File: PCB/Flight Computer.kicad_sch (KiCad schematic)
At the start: 0 parts

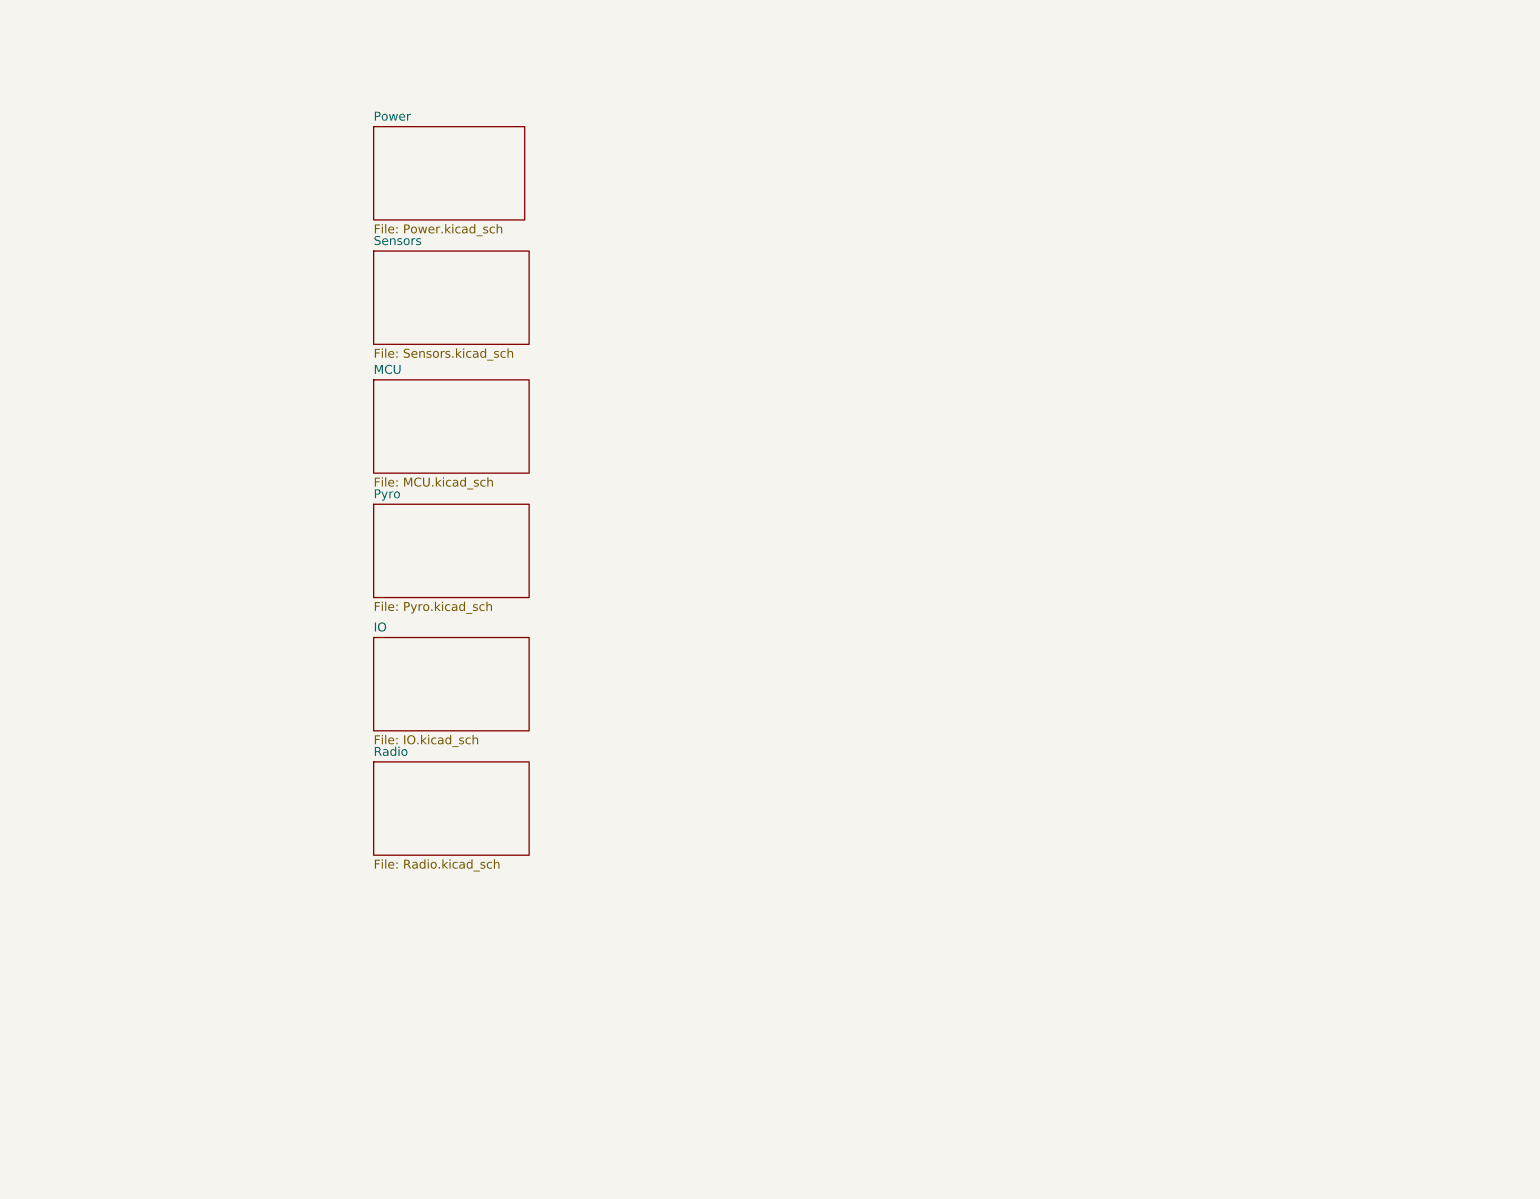
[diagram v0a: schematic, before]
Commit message: Cleaned up the schematic and replace and rerouted everything, also replace radio with a module
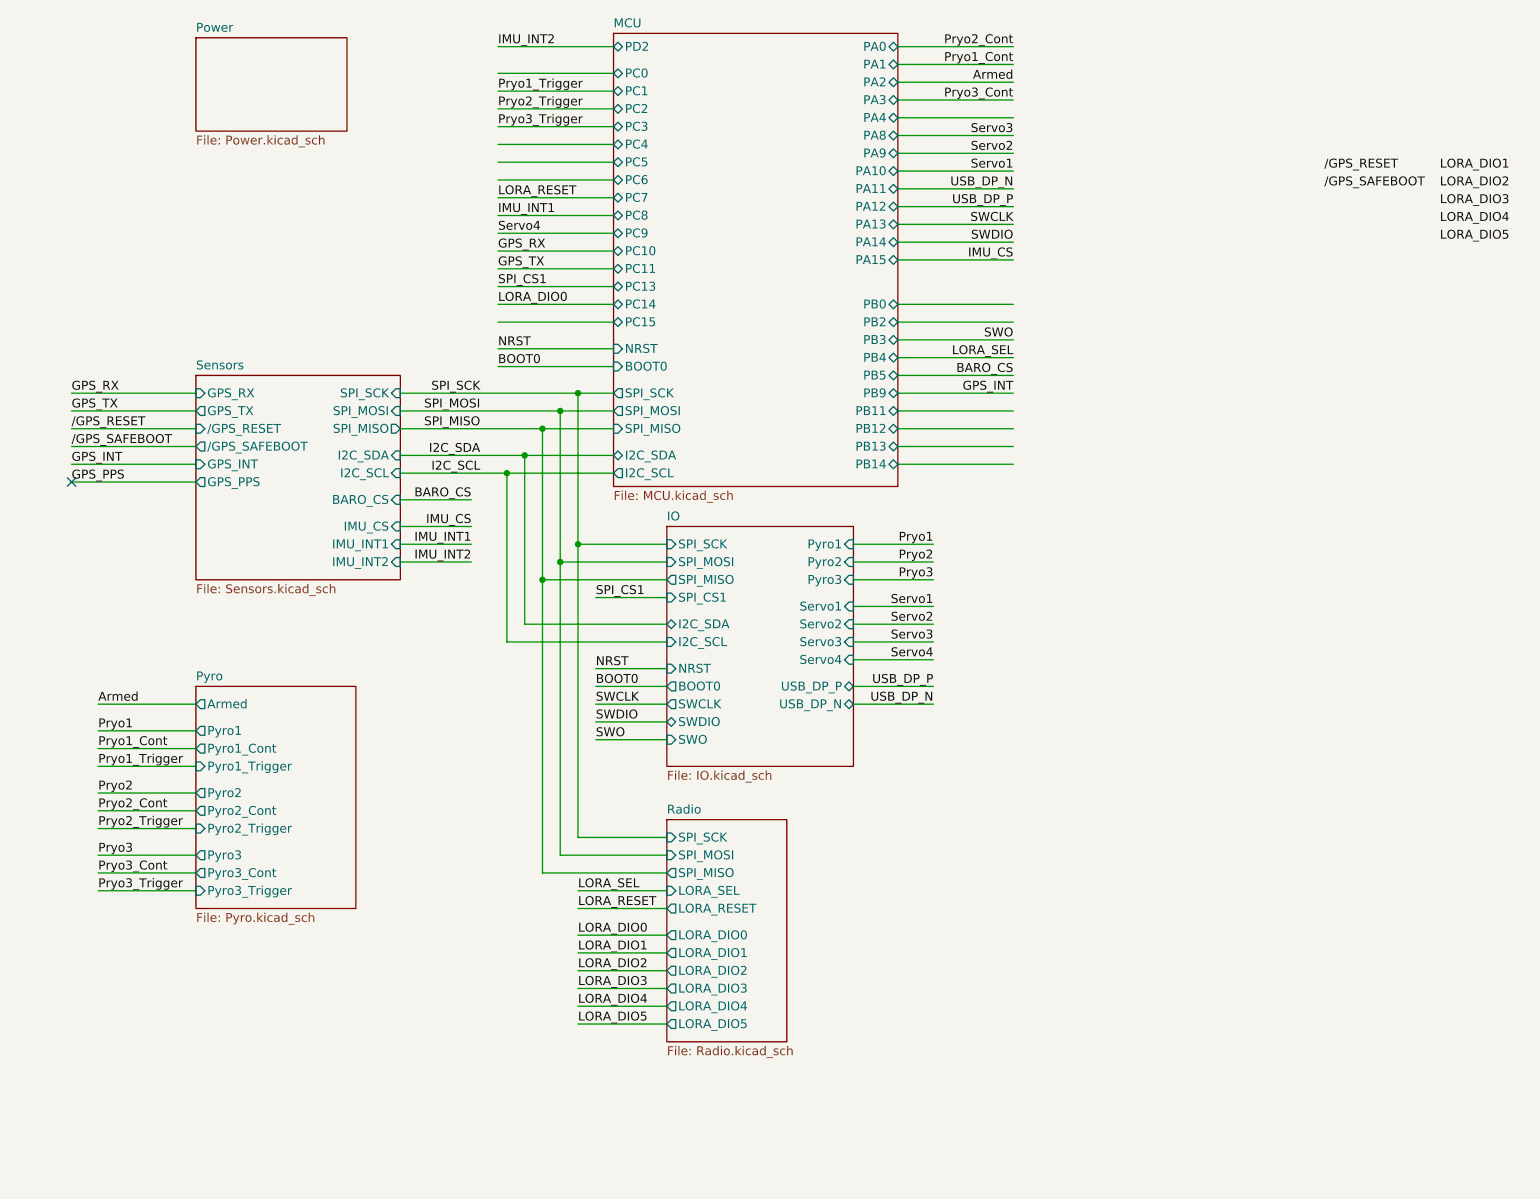
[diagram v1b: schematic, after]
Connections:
- no-connect marks 0 -> 1
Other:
- sheet IO ports: added BOOT0, I2C_SCL, I2C_SDA, NRST, Pyro1, Pyro2, Pyro3, SPI_CS1, SPI_MISO, SPI_MOSI, SPI_SCK, SWCLK, SWDIO, SWO, Servo1, Servo2, Servo3, Servo4, USB_DP_N, USB_DP_P; removed none
- sheet MCU ports: added BOOT0, I2C_SCL, I2C_SDA, NRST, PA0, PA1, PA10, PA11, PA12, PA13, PA14, PA15, PA2, PA3, PA4, PA8, PA9, PB0, PB11, PB12, PB13, PB14, PB2, PB3, PB4, PB5, PB9, PC0, PC1, PC10, PC11, PC13, PC14, PC15, PC2, PC3, PC4, PC5, PC6, PC7, PC8, PC9, PD2, SPI_MISO, SPI_MOSI, SPI_SCK; removed none
- sheet Pyro ports: added Armed, Pyro1, Pyro1_Cont, Pyro1_Trigger, Pyro2, Pyro2_Cont, Pyro2_Trigger, Pyro3, Pyro3_Cont, Pyro3_Trigger; removed none
- sheet Radio ports: added LORA_DIO0, LORA_DIO1, LORA_DIO2, LORA_DIO3, LORA_DIO4, LORA_DIO5, LORA_RESET, LORA_SEL, SPI_MISO, SPI_MOSI, SPI_SCK; removed none
- sheet Sensors ports: added BARO_CS, GPS_INT, GPS_PPS, GPS_RX, GPS_TX, I2C_SCL, I2C_SDA, IMU_CS, IMU_INT1, IMU_INT2, SPI_MISO, SPI_MOSI, SPI_SCK, /GPS_RESET, /GPS_SAFEBOOT; removed none

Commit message: Fixed barometer wiring
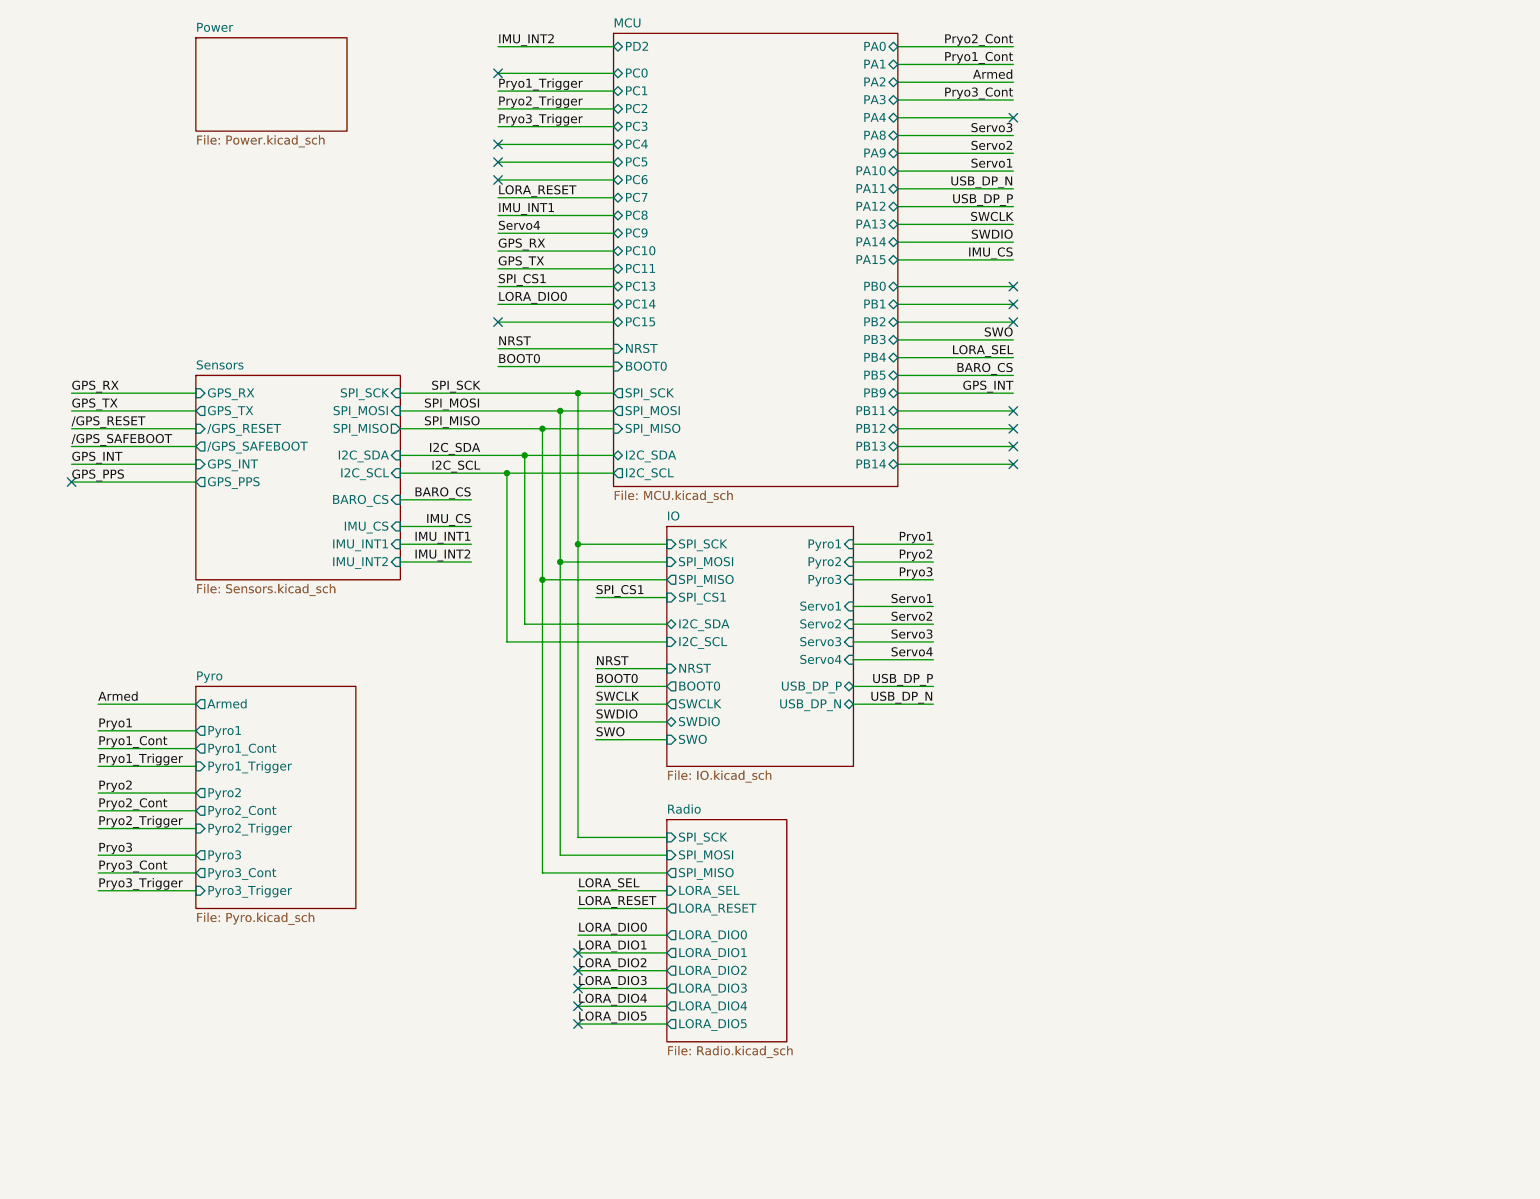
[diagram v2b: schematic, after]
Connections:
- no-connect marks 1 -> 19
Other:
- sheet MCU ports: added PB1; removed none
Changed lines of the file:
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@@
+	)
+	(no_connect
+		(at 173.99 68.58)
+	)
+	(no_connect
+		(at 173.99 91.44)
+	)
+	(no_connect
+		(at 173.99 66.04)
+	)
+	(no_connect
+		(at 111.76 161.29)
+	)
+	(no_connect
+		(at 173.99 83.82)
+	)
+	(no_connect
+		(at 100.33 45.72)
+	)
+	(no_connect
+		(at 100.33 71.12)
 	)
 	(no_connect
 		(at 39.37 93.98)
 	)
+	(no_connect
+		(at 111.76 163.83)
+	)
+	(no_connect
+		(at 173.99 71.12)
+	)
+	(no_connect
+		(at 173.99 88.9)
+	)
+	(no_connect
+		(at 111.76 168.91)
+	)
+	(no_connect
+		(at 111.76 171.45)
+	)
+	(no_connect
+		(at 100.33 48.26)
+	)
+	(no_connect
+		(at 173.99 86.36)
+	)
+	(no_connect
+		(at 173.99 41.91)
+	)
+	(no_connect
+		(at 100.33 35.56)
+	)
+	(no_connect
+		(at 111.76 166.37)
+	)
+	(no_connect
+		(at 100.33 50.8)
+	)
 	(wire
 		(pts
@@
 	(wire
 		(pts
+			(xy 157.48 68.58) (xy 173.99 68.58)
+		)
+		(stroke
+			(width 0)
+			(type default)
+		)
+	)
+	(wire
+		(pts
 			(xy 157.48 31.75) (xy 173.99 31.75)
 		)
@@
 	(wire
 		(pts
-			(xy 157.48 68.58) (xy 173.99 68.58)
+			(xy 157.48 66.04) (xy 173.99 66.04)
 		)
 		(stroke
@@
 		)
 	)
-	(label "LORA_DIO1"
-		(at 234.95 49.53 0)
-		(effects
-			(font
-				(size 1.27 1.27)
-			)
-			(justify left bottom)
-		)
-	)
 	(label "IMU_INT1"
 		(at 100.33 55.88 0)
@@
 		)
 	)
-	(label "LORA_DIO5"
-		(at 234.95 59.69 0)
-		(effects
-			(font
-				(size 1.27 1.27)
-			)
-			(justify left bottom)
-		)
-	)
-	(label "{slash}GPS_SAFEBOOT"
-		(at 218.44 52.07 0)
-		(effects
-			(font
-				(size 1.27 1.27)
-			)
-			(justify left bottom)
-		)
-	)
 	(label "GPS_TX"
 		(at 100.33 63.5 0)
@@
 		)
 	)
-	(label "LORA_DIO3"
-		(at 234.95 54.61 0)
-		(effects
-			(font
-				(size 1.27 1.27)
-			)
-			(justify left bottom)
-		)
-	)
 	(label "Pryo2_Cont"
 		(at 173.99 31.75 180)
@@
 		)
 	)
-	(label "LORA_DIO2"
-		(at 234.95 52.07 0)
-		(effects
-			(font
-				(size 1.27 1.27)
-			)
-			(justify left bottom)
-		)
-	)
 	(label "LORA_DIO0"
 		(at 111.76 158.75 0)
@@
 		)
 	)
-	(label "{slash}GPS_RESET"
-		(at 218.44 49.53 0)
-		(effects
-			(font
-				(size 1.27 1.27)
-			)
-			(justify left bottom)
-		)
-	)
 	(label "NRST"
 		(at 100.33 74.93 0)
@@
 			)
 			(justify right bottom)
-		)
-	)
-	(label "LORA_DIO4"
-		(at 234.95 57.15 0)
-		(effects
-			(font
-				(size 1.27 1.27)
-			)
-			(justify left bottom)
 		)
 	)
@@
 		)
 		(pin "PB0" bidirectional
-			(at 157.48 68.58 0)
+			(at 157.48 66.04 0)
 			(effects
 				(font
@@
 			(effects
 				(font
+					(size 1.27 1.27)
+				)
+				(justify right)
+			)
+		)
+		(pin "PB1" bidirectional
+			(at 157.48 68.58 0)
+			(effects
+				(font

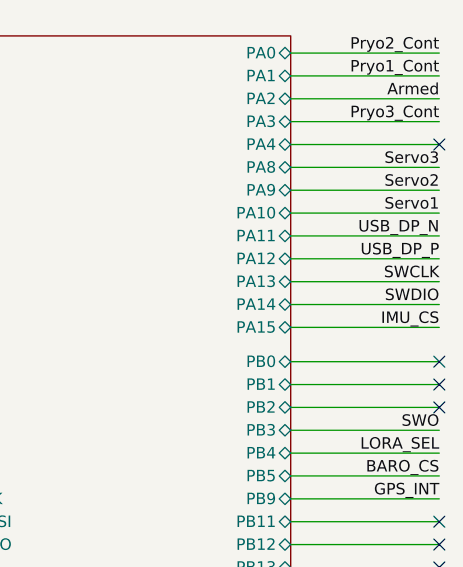
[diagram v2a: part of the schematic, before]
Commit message: Fixed SWD pinout Updated CubeMX Project
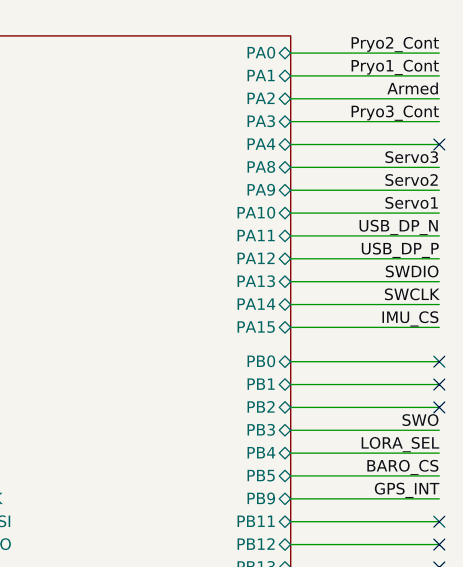
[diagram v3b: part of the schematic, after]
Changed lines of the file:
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@@
 	)
 	(label "SWCLK"
-		(at 173.99 57.15 180)
+		(at 173.99 59.69 180)
 		(effects
 			(font
@@
 	)
 	(label "SWDIO"
-		(at 173.99 59.69 180)
-		(effects
-			(font
+		(at 173.99 57.15 180)
+		(effects
+			(font

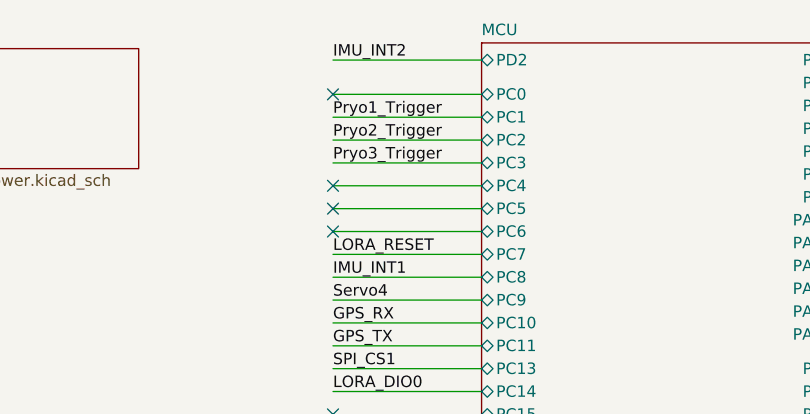
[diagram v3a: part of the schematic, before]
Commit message: Redid layout to make it look a little nicer Added some silkscreen to connectors
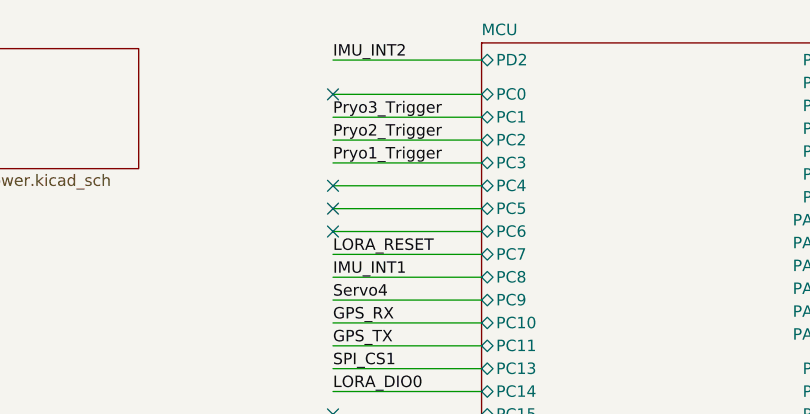
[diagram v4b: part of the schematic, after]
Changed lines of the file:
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@@
 	)
 	(label "Pryo1_Trigger"
-		(at 100.33 38.1 0)
+		(at 100.33 43.18 0)
 		(effects
 			(font
@@
 	)
 	(label "Pryo3_Trigger"
-		(at 100.33 43.18 0)
+		(at 100.33 38.1 0)
 		(effects
 			(font
